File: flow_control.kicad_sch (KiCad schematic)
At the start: 62 parts, among them J10 Pump 1, J11 Temperature, J12 Pump 2, J13 Pump 3, J3 Flow, J7 Valve 1, J8 Valve 2, J9 Valve 3, Q1 MMBT3904, Q10 AO3401A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

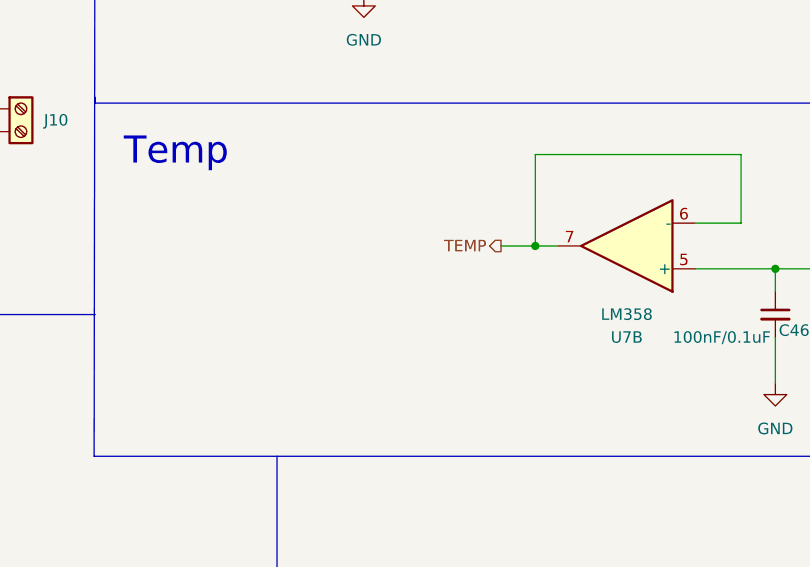
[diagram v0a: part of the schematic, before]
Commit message: Add dampening on NTC temp signal
STM32 input is not 5V tolerant so the signal is lowered to 3.3V
Closes #36
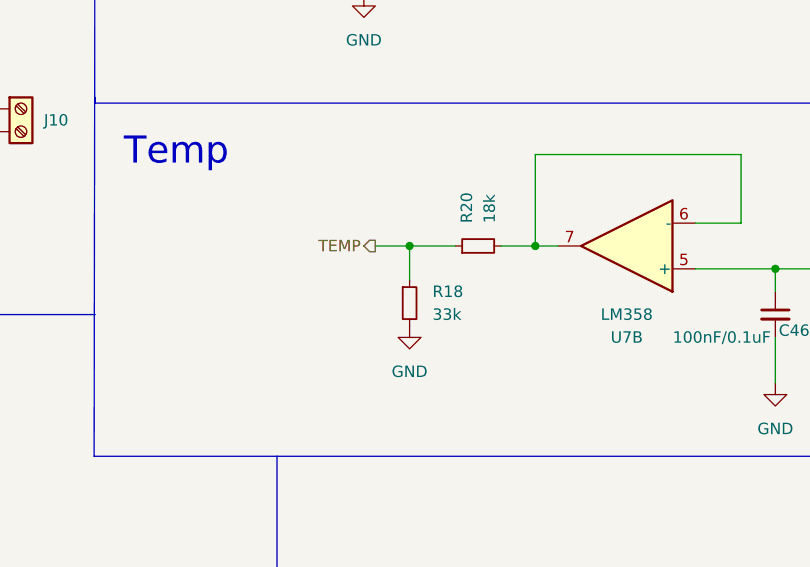
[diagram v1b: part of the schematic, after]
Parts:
- added R18: 33k, Resistor_SMD:R_0603_1608Metric, symbol Device:R_Small
- added R20: 18k, Resistor_SMD:R_0603_1608Metric, symbol Device:R_Small
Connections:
- net GND: now also R18.2
- net TEMP: now also R18.1, R20.1; no longer U7.6 (-), U7.7
- new net: R20.2, U7.6 (-), U7.7

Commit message: Update part for JST 2P connectors
Closes #41
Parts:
- J11: LCSC C493111 -> C157931; LCSC alt (none) -> C493111
- J7, J8: LCSC C493111 -> C157931
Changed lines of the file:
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@@
 			)
 		)
-		(property "LCSC" "C493111"
+		(property "LCSC" "C157931"
 			(at 76.2 127 0)
 			(effects
@@
 			)
 		)
-		(property "LCSC" "C493111"
+		(property "LCSC" "C157931"
 			(at 76.2 176.53 0)
 			(effects
@@
 			)
 		)
-		(property "LCSC alt" ""
+		(property "LCSC" "C157931"
 			(at 267.97 80.01 0)
 			(effects
@@
 			)
 		)
-		(property "LCSC" "C493111"
+		(property "LCSC alt" "C493111"
 			(at 267.97 80.01 0)
 			(effects

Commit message: Update manufacturing positions and rotations of parts
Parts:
- J10, J12, J13: JLCPCB Position Offset (none) -> 0,3
- J11, J3, J7, J8, J9: JLCPCB Position Offset (none) -> 0,3.5; JLCPCB Rotation Offset (none) -> 180
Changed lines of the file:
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@@
 			)
 		)
+		(property "JLCPCB Position Offset" "0,3"
+			(at 148.59 176.53 0)
+			(effects
+				(font
+					(size 1.27 1.27)
+				)
+				(hide yes)
+			)
+		)
 		(pin "2"
 		)
@@
 			)
 		)
+		(property "JLCPCB Position Offset" "0,3"
+			(at 148.59 127 0)
+			(effects
+				(font
+					(size 1.27 1.27)
+				)
+				(hide yes)
+			)
+		)
 		(pin "2"
 		)
@@
 			)
 		)
+		(property "JLCPCB Position Offset" "0,3.5"
+			(at 76.2 127 0)
+			(effects
+				(font
+					(size 1.27 1.27)
+				)
+				(hide yes)
+			)
+		)
+		(property "JLCPCB Rotation Offset" "180"
+			(at 76.2 127 0)
+			(effects
+				(font
+					(size 1.27 1.27)
+				)
+				(hide yes)
+			)
+		)
 		(pin "2"
 		)
@@
 			)
 		)
+		(property "JLCPCB Position Offset" "0,3.5"
+			(at 76.2 176.53 0)
+			(effects
+				(font
+					(size 1.27 1.27)
+				)
+				(hide yes)
+			)
+		)
+		(property "JLCPCB Rotation Offset" "180"
+			(at 76.2 176.53 0)
+			(effects
+				(font
+					(size 1.27 1.27)
+				)
+				(hide yes)
+			)
+		)
 		(pin "2"
 		)
@@
 			)
 		)
+		(property "JLCPCB Position Offset" "0,3.5"
+			(at 267.97 80.01 0)
+			(effects
+				(font
+					(size 1.27 1.27)
+				)
+				(hide yes)
+			)
+		)
+		(property "JLCPCB Rotation Offset" "180"
+			(at 267.97 80.01 0)
+			(effects
+				(font
+					(size 1.27 1.27)
+				)
+				(hide yes)
+			)
+		)
 		(pin "1"
 		)
@@
 			)
 		)
+		(property "JLCPCB Position Offset" "0,3.5"
+			(at 267.97 35.56 0)
+			(effects
+				(font
+					(size 1.27 1.27)
+				)
+				(hide yes)
+			)
+		)
+		(property "JLCPCB Rotation Offset" "180"
+			(at 267.97 35.56 0)
+			(effects
+				(font
+					(size 1.27 1.27)
+				)
+				(hide yes)
+			)
+		)
 		(pin "2"
 		)
@@
 			)
 		)
+		(property "JLCPCB Position Offset" "0,3"
+			(at 148.59 62.23 0)
+			(effects
+				(font
+					(size 1.27 1.27)
+				)
+				(hide yes)
+			)
+		)
 		(pin "2"
 		)
@@
 			(at 80.01 77.47 0)
 			(effects
+				(font
+					(size 1.27 1.27)
+				)
+				(hide yes)
+			)
+		)
+		(property "JLCPCB Position Offset" "0,3.5"
+			(at 80.01 77.47 0)
+			(effects
+				(font
+					(size 1.27 1.27)
+				)
+				(hide yes)
+			)
+		)
+		(property "JLCPCB Rotation Offset" "180"
+			(at 80.01 77.47 0)
+			(effects

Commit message: Include THT components in manufacturing
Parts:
- J10, J11, J12, J13, J3, J7, J8, J9: now in the parts list
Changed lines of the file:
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@@
 		(unit 1)
 		(exclude_from_sim no)
-		(in_bom no)
+		(in_bom yes)
 		(on_board yes)
 		(dnp no)
@@
 		(unit 1)
 		(exclude_from_sim no)
-		(in_bom no)
+		(in_bom yes)
 		(on_board yes)
 		(dnp no)
@@
 		(unit 1)
 		(exclude_from_sim no)
-		(in_bom no)
+		(in_bom yes)
 		(on_board yes)
 		(dnp no)
@@
 		(unit 1)
 		(exclude_from_sim no)
-		(in_bom no)
+		(in_bom yes)
 		(on_board yes)
 		(dnp no)
@@
 		(unit 1)
 		(exclude_from_sim no)
-		(in_bom no)
+		(in_bom yes)
 		(on_board yes)
 		(dnp no)
@@
 		(unit 1)
 		(exclude_from_sim no)
-		(in_bom no)
+		(in_bom yes)
 		(on_board yes)
 		(dnp no)
@@
 		(unit 1)
 		(exclude_from_sim no)
-		(in_bom no)
+		(in_bom yes)
 		(on_board yes)
 		(dnp no)
@@
 		(unit 1)
 		(exclude_from_sim no)
-		(in_bom no)
+		(in_bom yes)
 		(on_board yes)
 		(dnp no)
